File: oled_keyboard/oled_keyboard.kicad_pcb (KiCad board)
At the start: 2 copper layers, 125 x 125 mm, 123 parts, among them J1 Conn_01x20_Socket, J10 Conn_01x20_Socket, J11 Conn_01x20_Socket, J12 Conn_01x20_Socket, J2 Conn_01x20_Socket, J3 Conn_01x20_Socket, J4 Conn_01x20_Socket, J5 Conn_01x20_Socket, J6 Conn_01x20_Socket, J7 Conn_01x20_Socket, J8 Conn_01x20_Socket, J9 Conn_01x20_Socket, SW1 SW_Push, SW10 SW_Push, SW11 SW_Push, SW12 SW_Push, SW2 SW_Push, SW3 SW_Push, SW4 SW_Push, SW5 SW_Push, SW6 SW_Push, SW7 SW_Push, SW8 SW_Push, SW9 SW_Push, U1 TPS61088RHLR

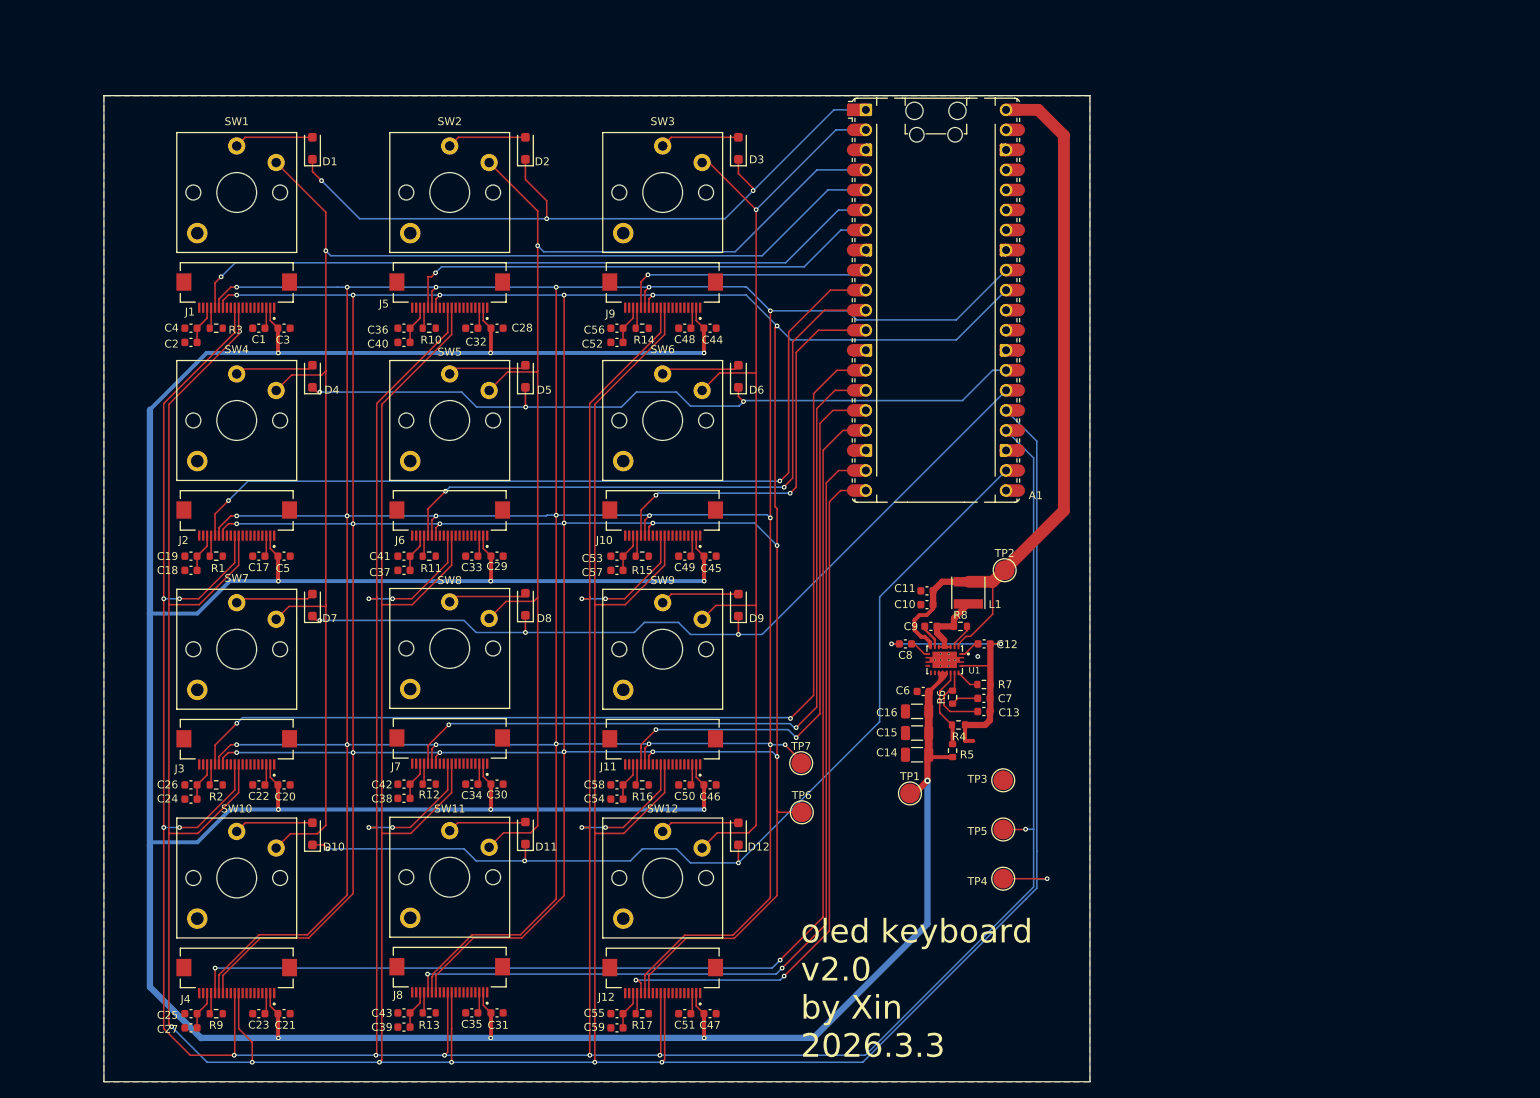
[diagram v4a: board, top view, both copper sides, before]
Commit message: chged to 9 oled. fixed pin inversion issue
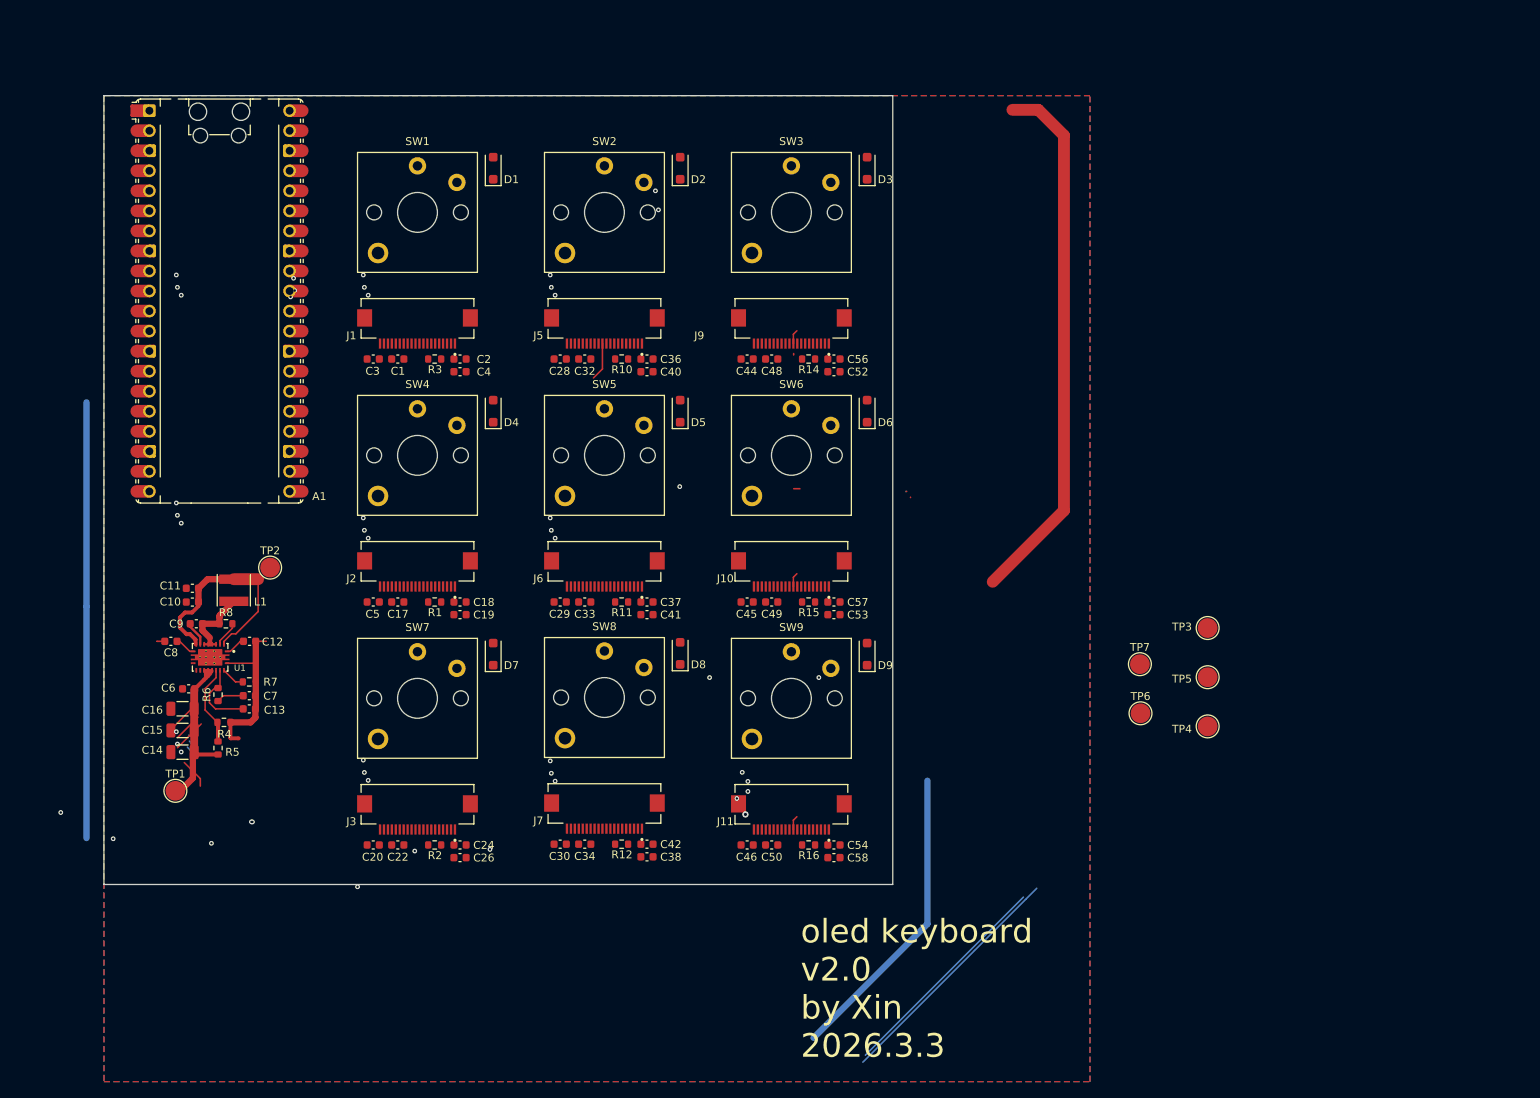
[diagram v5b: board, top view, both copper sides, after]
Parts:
- removed C21, C23, C31, C35, C47, C51: 4.7uF, Capacitor_SMD:C_0603_1608Metric
- removed C25, C39, C55: 0.1uF, Capacitor_SMD:C_0603_1608Metric
- removed C27, C43, C59: 1uF, Capacitor_SMD:C_0603_1608Metric
- removed D10, D11, D12: D, Diode_SMD:D_SOD-123F
- removed J12, J4, J8: Conn_01x20_Socket, 20p_connector:HRS_TF31-20S-0.5SH_800_
- removed R13, R17, R9: 1M, Resistor_SMD:R_0603_1608Metric
- removed SW10, SW11, SW12: SW_Push, Switch_Keyboard_Kailh:SW_Kailh_Choc_V1V2
- moved C10 93.1 mm to (93.1, 94.7)
- moved C11 93.1 mm to (93.1, 93.0)
- moved C12 93.1 mm to (100.3, 99.7)
- moved C13 93.1 mm to (100.3, 108.2)
- moved C14 93.1 mm to (91.8, 113.7)
- moved C15 93.1 mm to (91.8, 111.0)
- moved C16 93.1 mm to (91.8, 108.2)
- moved C7 93.1 mm to (100.3, 106.6)
- moved C9 93.1 mm to (93.6, 97.5)
- moved L1 93.1 mm to (98.3, 93.2)
- moved NT1 93.1 mm to (98.4, 112.0)
- moved R4 93.1 mm to (97.1, 110.0)
- moved R5 93.1 mm to (96.3, 113.2)
- moved R6 93.1 mm to (96.3, 106.4)
- moved R7 93.1 mm to (100.3, 104.8)
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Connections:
- C1 pad 1: Net-(J1-Pin_3) -> Net-(J1-Pin_18)
- C17 pad 1: Net-(J2-Pin_3) -> Net-(J2-Pin_18)
- C18 pad 1: Net-(J2-Pin_18) -> Net-(J2-Pin_3)
- C19 pad 1: Net-(J2-Pin_18) -> Net-(J2-Pin_3)
- C2 pad 1: Net-(J1-Pin_18) -> Net-(J1-Pin_3)
- C22 pad 1: Net-(J3-Pin_3) -> Net-(J3-Pin_18)
- C24 pad 1: Net-(J3-Pin_18) -> Net-(J3-Pin_3)
- C26 pad 1: Net-(J3-Pin_18) -> Net-(J3-Pin_3)
- C32 pad 1: Net-(J5-Pin_3) -> Net-(J5-Pin_18)
- C33 pad 1: Net-(J6-Pin_3) -> Net-(J6-Pin_18)
- C34 pad 1: Net-(J7-Pin_3) -> Net-(J7-Pin_18)
- C36 pad 1: Net-(J5-Pin_18) -> Net-(J5-Pin_3)
- C37 pad 1: Net-(J6-Pin_18) -> Net-(J6-Pin_3)
- C38 pad 1: Net-(J7-Pin_18) -> Net-(J7-Pin_3)
- C4 pad 1: Net-(J1-Pin_18) -> Net-(J1-Pin_3)
- C40 pad 1: Net-(J5-Pin_18) -> Net-(J5-Pin_3)
- C41 pad 1: Net-(J6-Pin_18) -> Net-(J6-Pin_3)
- C42 pad 1: Net-(J7-Pin_18) -> Net-(J7-Pin_3)
- C48 pad 1: Net-(J9-Pin_3) -> Net-(J9-Pin_18)
- C49 pad 1: Net-(J10-Pin_3) -> Net-(J10-Pin_18)
- C50 pad 1: Net-(J11-Pin_3) -> Net-(J11-Pin_18)
- C52 pad 1: Net-(J9-Pin_18) -> Net-(J9-Pin_3)
- C53 pad 1: Net-(J10-Pin_18) -> Net-(J10-Pin_3)
- C54 pad 1: Net-(J11-Pin_18) -> Net-(J11-Pin_3)
- C56 pad 1: Net-(J9-Pin_18) -> Net-(J9-Pin_3)
- C57 pad 1: Net-(J10-Pin_18) -> Net-(J10-Pin_3)
- C58 pad 1: Net-(J11-Pin_18) -> Net-(J11-Pin_3)
- J1 pad 10: /MOSI -> /SCK
- J1 pad 11: /SCK -> /MOSI
- J1 pad 14: /DC -> unconnected-(J1-Pin_14-Pad14)
- J1 pad 15: /RES -> unconnected-(J1-Pin_15-Pad15)
- J1 pad 16: /CS1 -> unconnected-(J1-Pin_16-Pad16)
- J1 pad 17: Net-(J1-Pin_17) -> unconnected-(J1-Pin_17-Pad17)
- J1 pad 19: unconnected-(J1-Pin_19-Pad19) -> VCC
- J1 pad 2: VCC -> unconnected-(J1-Pin_2-Pad2)
- J1 pad 4: unconnected-(J1-Pin_4-Pad4) -> Net-(J1-Pin_4)
- J1 pad 5: unconnected-(J1-Pin_5-Pad5) -> /CS1
- J1 pad 6: unconnected-(J1-Pin_6-Pad6) -> /RES
- J1 pad 7: unconnected-(J1-Pin_7-Pad7) -> /DC
- J10 pad 10: /MOSI -> /SCK
- J10 pad 11: /SCK -> /MOSI
- J10 pad 14: /DC -> unconnected-(J10-Pin_14-Pad14)
- J10 pad 15: /RES -> unconnected-(J10-Pin_15-Pad15)
- J10 pad 16: /CS6 -> unconnected-(J10-Pin_16-Pad16)
- J10 pad 17: Net-(J10-Pin_17) -> unconnected-(J10-Pin_17-Pad17)
- J10 pad 19: unconnected-(J10-Pin_19-Pad19) -> VCC
- J10 pad 2: VCC -> unconnected-(J10-Pin_2-Pad2)
- J10 pad 4: unconnected-(J10-Pin_4-Pad4) -> Net-(J10-Pin_4)
- J10 pad 5: unconnected-(J10-Pin_5-Pad5) -> /CS6
- J10 pad 6: unconnected-(J10-Pin_6-Pad6) -> /RES
- J10 pad 7: unconnected-(J10-Pin_7-Pad7) -> /DC
- J11 pad 10: /MOSI -> /SCK
- J11 pad 11: /SCK -> /MOSI
- J11 pad 14: /DC -> unconnected-(J11-Pin_14-Pad14)
- J11 pad 15: /RES -> unconnected-(J11-Pin_15-Pad15)
- J11 pad 16: /CS9 -> unconnected-(J11-Pin_16-Pad16)
- J11 pad 17: Net-(J11-Pin_17) -> unconnected-(J11-Pin_17-Pad17)
- J11 pad 19: unconnected-(J11-Pin_19-Pad19) -> VCC
- J11 pad 2: VCC -> unconnected-(J11-Pin_2-Pad2)
- J11 pad 4: unconnected-(J11-Pin_4-Pad4) -> Net-(J11-Pin_4)
- J11 pad 5: unconnected-(J11-Pin_5-Pad5) -> /CS9
- J11 pad 6: unconnected-(J11-Pin_6-Pad6) -> /RES
- J11 pad 7: unconnected-(J11-Pin_7-Pad7) -> /DC
- J2 pad 10: /MOSI -> /SCK
- J2 pad 11: /SCK -> /MOSI
- J2 pad 14: /DC -> unconnected-(J2-Pin_14-Pad14)
- J2 pad 15: /RES -> unconnected-(J2-Pin_15-Pad15)
- J2 pad 16: /CS4 -> unconnected-(J2-Pin_16-Pad16)
- J2 pad 17: Net-(J2-Pin_17) -> unconnected-(J2-Pin_17-Pad17)
- J2 pad 19: unconnected-(J2-Pin_19-Pad19) -> VCC
- J2 pad 2: VCC -> unconnected-(J2-Pin_2-Pad2)
- J2 pad 4: unconnected-(J2-Pin_4-Pad4) -> Net-(J2-Pin_4)
- J2 pad 5: unconnected-(J2-Pin_5-Pad5) -> /CS4
- J2 pad 6: unconnected-(J2-Pin_6-Pad6) -> /RES
- J2 pad 7: unconnected-(J2-Pin_7-Pad7) -> /DC
- J3 pad 10: /MOSI -> /SCK
- J3 pad 11: /SCK -> /MOSI
- J3 pad 14: /DC -> unconnected-(J3-Pin_14-Pad14)
- J3 pad 15: /RES -> unconnected-(J3-Pin_15-Pad15)
- J3 pad 16: /CS7 -> unconnected-(J3-Pin_16-Pad16)
- J3 pad 17: Net-(J3-Pin_17) -> unconnected-(J3-Pin_17-Pad17)
- J3 pad 19: unconnected-(J3-Pin_19-Pad19) -> VCC
- J3 pad 2: VCC -> unconnected-(J3-Pin_2-Pad2)
- J3 pad 4: unconnected-(J3-Pin_4-Pad4) -> Net-(J3-Pin_4)
- J3 pad 5: unconnected-(J3-Pin_5-Pad5) -> /CS7
- J3 pad 6: unconnected-(J3-Pin_6-Pad6) -> /RES
- J3 pad 7: unconnected-(J3-Pin_7-Pad7) -> /DC
- J5 pad 10: /MOSI -> /SCK
- J5 pad 11: /SCK -> /MOSI
- J5 pad 14: /DC -> unconnected-(J5-Pin_14-Pad14)
- J5 pad 15: /RES -> unconnected-(J5-Pin_15-Pad15)
- J5 pad 16: /CS2 -> unconnected-(J5-Pin_16-Pad16)
- J5 pad 17: Net-(J5-Pin_17) -> unconnected-(J5-Pin_17-Pad17)
- J5 pad 19: unconnected-(J5-Pin_19-Pad19) -> VCC
- J5 pad 2: VCC -> unconnected-(J5-Pin_2-Pad2)
- J5 pad 4: unconnected-(J5-Pin_4-Pad4) -> Net-(J5-Pin_4)
- J5 pad 5: unconnected-(J5-Pin_5-Pad5) -> /CS2
- J5 pad 6: unconnected-(J5-Pin_6-Pad6) -> /RES
- J5 pad 7: unconnected-(J5-Pin_7-Pad7) -> /DC
- J6 pad 10: /MOSI -> /SCK
- J6 pad 11: /SCK -> /MOSI
- J6 pad 14: /DC -> unconnected-(J6-Pin_14-Pad14)
- J6 pad 15: /RES -> unconnected-(J6-Pin_15-Pad15)
- J6 pad 16: /CS5 -> unconnected-(J6-Pin_16-Pad16)
- J6 pad 17: Net-(J6-Pin_17) -> unconnected-(J6-Pin_17-Pad17)
- J6 pad 19: unconnected-(J6-Pin_19-Pad19) -> VCC
- J6 pad 2: VCC -> unconnected-(J6-Pin_2-Pad2)
- J6 pad 4: unconnected-(J6-Pin_4-Pad4) -> Net-(J6-Pin_4)
- J6 pad 5: unconnected-(J6-Pin_5-Pad5) -> /CS5
- J6 pad 6: unconnected-(J6-Pin_6-Pad6) -> /RES
- J6 pad 7: unconnected-(J6-Pin_7-Pad7) -> /DC
- J7 pad 10: /MOSI -> /SCK
- J7 pad 11: /SCK -> /MOSI
- J7 pad 14: /DC -> unconnected-(J7-Pin_14-Pad14)
- J7 pad 15: /RES -> unconnected-(J7-Pin_15-Pad15)
- J7 pad 16: /CS8 -> unconnected-(J7-Pin_16-Pad16)
- J7 pad 17: Net-(J7-Pin_17) -> unconnected-(J7-Pin_17-Pad17)
- J7 pad 19: unconnected-(J7-Pin_19-Pad19) -> VCC
- J7 pad 2: VCC -> unconnected-(J7-Pin_2-Pad2)
- J7 pad 4: unconnected-(J7-Pin_4-Pad4) -> Net-(J7-Pin_4)
- J7 pad 5: unconnected-(J7-Pin_5-Pad5) -> /CS8
- J7 pad 6: unconnected-(J7-Pin_6-Pad6) -> /RES
- J7 pad 7: unconnected-(J7-Pin_7-Pad7) -> /DC
- J9 pad 10: /MOSI -> /SCK
- J9 pad 11: /SCK -> /MOSI
- J9 pad 14: /DC -> unconnected-(J9-Pin_14-Pad14)
- J9 pad 15: /RES -> unconnected-(J9-Pin_15-Pad15)
- J9 pad 16: /CS3 -> unconnected-(J9-Pin_16-Pad16)
- J9 pad 17: Net-(J9-Pin_17) -> unconnected-(J9-Pin_17-Pad17)
- J9 pad 19: unconnected-(J9-Pin_19-Pad19) -> VCC
- J9 pad 2: VCC -> unconnected-(J9-Pin_2-Pad2)
- J9 pad 4: unconnected-(J9-Pin_4-Pad4) -> Net-(J9-Pin_4)
- J9 pad 5: unconnected-(J9-Pin_5-Pad5) -> /CS3
- J9 pad 6: unconnected-(J9-Pin_6-Pad6) -> /RES
- J9 pad 7: unconnected-(J9-Pin_7-Pad7) -> /DC
- R1 pad 1: Net-(J2-Pin_17) -> Net-(J2-Pin_4)
- R10 pad 1: Net-(J5-Pin_17) -> Net-(J5-Pin_4)
- R11 pad 1: Net-(J6-Pin_17) -> Net-(J6-Pin_4)
- R12 pad 1: Net-(J7-Pin_17) -> Net-(J7-Pin_4)
- R14 pad 1: Net-(J9-Pin_17) -> Net-(J9-Pin_4)
- R15 pad 1: Net-(J10-Pin_17) -> Net-(J10-Pin_4)
- R16 pad 1: Net-(J11-Pin_17) -> Net-(J11-Pin_4)
- R2 pad 1: Net-(J3-Pin_17) -> Net-(J3-Pin_4)
- R3 pad 1: Net-(J1-Pin_17) -> Net-(J1-Pin_4)
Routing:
- net /RES: track 568.3 -> 3.82 mm, vias 19 -> 4
- net /MOSI: track 598.5 -> 36.0 mm, vias 7 -> 4
- net /DC: track 556.7 -> 0.00 mm, vias 18 -> 10
- net /SCK: track 594.2 -> 89.4 mm, vias 18 -> 9
- net VCC: track 513.8 -> 62.3 mm, vias 13 -> 2
- net /COL1: track 180.8 -> 0.00 mm, vias 1 -> 0
- net /COL2: track 154.4 -> 0.00 mm, vias 1 -> 0
- net /CS10: track 147.8 -> 0.00 mm, vias 2 -> 0
- net /COL3: track 128.8 -> 0.00 mm
- net /CS7: track 126.5 -> 0.00 mm, vias 2 -> 1
- net /ROW4: track 124.5 -> 0.00 mm, vias 3 -> 2
- net /CS11: track 116.4 -> 0.18 mm, vias 2 -> 1
- net /ROW3: track 107.3 -> 0.00 mm, vias 3 -> 0
- net /CS4: track 106.6 -> 0.00 mm, vias 2 -> 1
- net /ROW2: track 96.9 -> 0.00 mm, vias 3 -> 0
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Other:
- board size 125 x 125 mm -> 100 x 100 mm

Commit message: optimized key layout
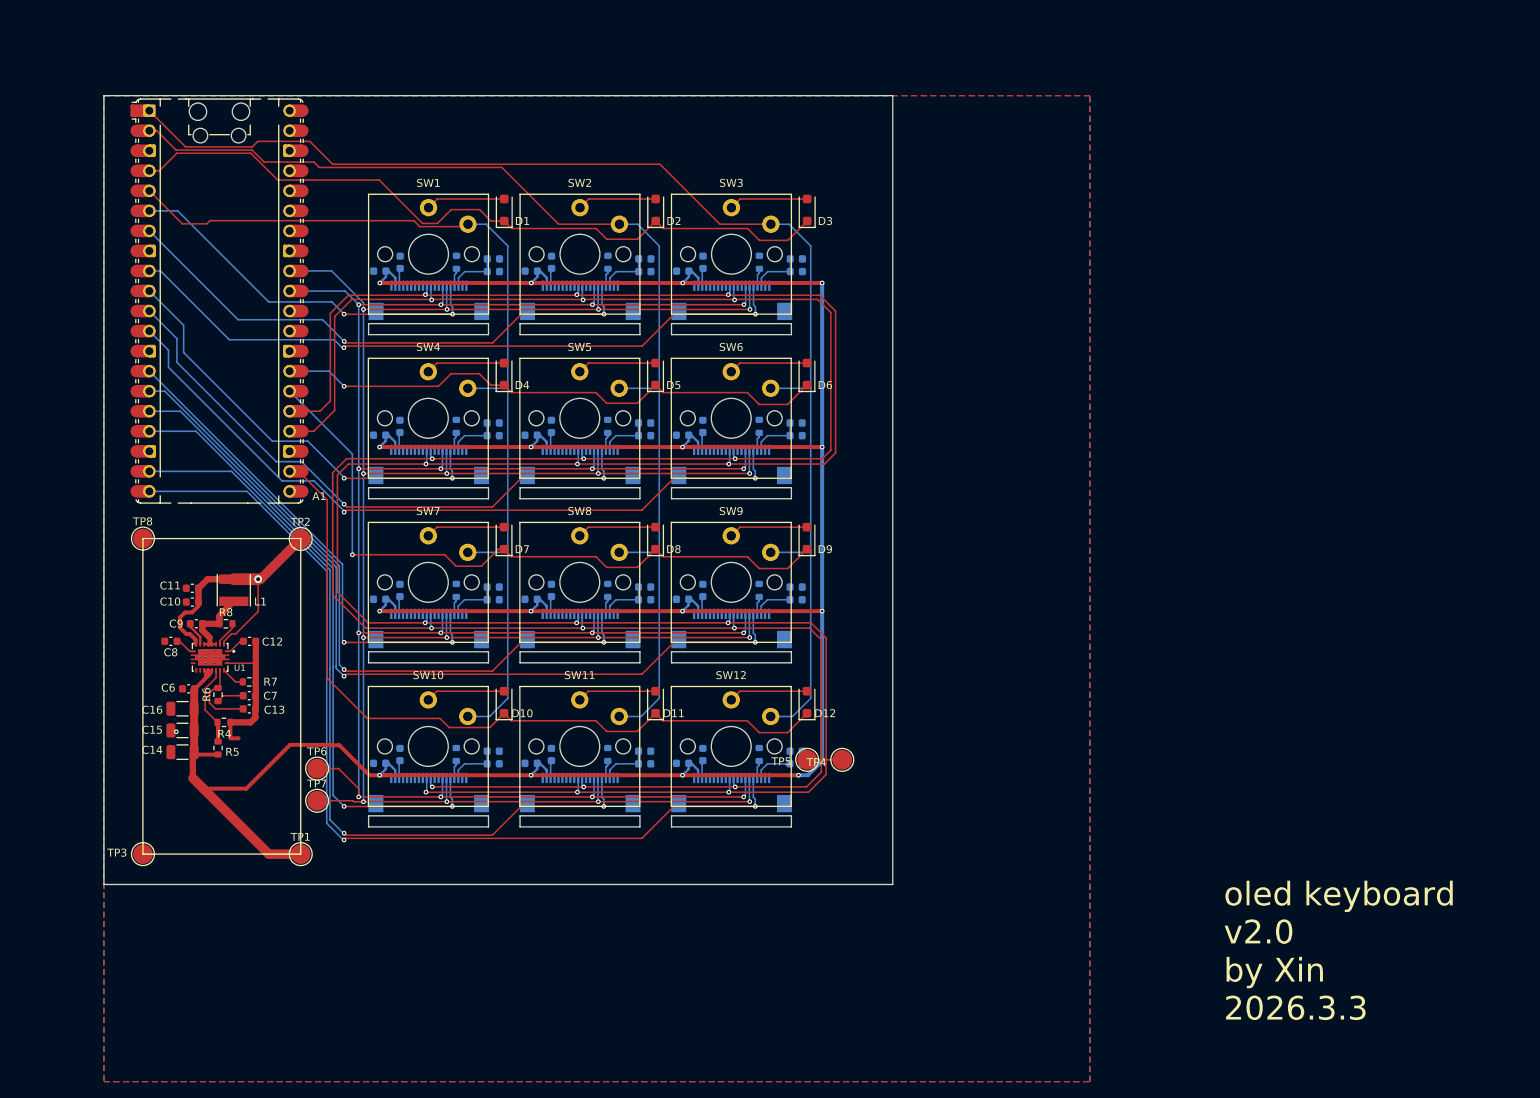
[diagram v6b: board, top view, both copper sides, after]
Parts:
- added C21: 1uF, Capacitor_SMD:C_0603_1608Metric, B.Cu at (131.2, 113.6)
- added C23: 0.1uF, Capacitor_SMD:C_0603_1608Metric, B.Cu at (131.2, 115.2)
- added C25: 4.7uF, Capacitor_SMD:C_0603_1608Metric, B.Cu at (119.4, 114.0)
- added C27: 4.7uF, Capacitor_SMD:C_0603_1608Metric, B.Cu at (116.8, 115.1)
- added C31: 1uF, Capacitor_SMD:C_0603_1608Metric, B.Cu at (150.4, 113.6)
- added C35: 0.1uF, Capacitor_SMD:C_0603_1608Metric, B.Cu at (150.4, 115.2)
- added C39: 4.7uF, Capacitor_SMD:C_0603_1608Metric, B.Cu at (138.6, 114.0)
- added C43: 4.7uF, Capacitor_SMD:C_0603_1608Metric, B.Cu at (136.0, 115.1)
- added C47: 1uF, Capacitor_SMD:C_0603_1608Metric, B.Cu at (169.6, 113.6)
- added C51: 0.1uF, Capacitor_SMD:C_0603_1608Metric, B.Cu at (169.6, 115.2)
- added C55: 4.7uF, Capacitor_SMD:C_0603_1608Metric, B.Cu at (157.8, 114.0)
- added C59: 4.7uF, Capacitor_SMD:C_0603_1608Metric, B.Cu at (155.2, 115.1)
- added D10: D, Diode_SMD:D_SOD-123F, F.Cu at (132.6, 107.4)
- added D11: D, Diode_SMD:D_SOD-123F, F.Cu at (151.8, 107.4)
- added D12: D, Diode_SMD:D_SOD-123F, F.Cu at (171.0, 107.4)
- added J12: Conn_01x20_Socket, 20pin_connector:HRS_TF31-20S-0.5SH_800_, B.Cu at (161.4, 120.2)
- added J4: Conn_01x20_Socket, 20pin_connector:HRS_TF31-20S-0.5SH_800_, B.Cu at (123.0, 120.2)
- added J8: Conn_01x20_Socket, 20pin_connector:HRS_TF31-20S-0.5SH_800_, B.Cu at (142.2, 120.2)
- added R13: 1M, Resistor_SMD:R_0603_1608Metric, B.Cu at (145.7, 114.0)
- added R17: 1M, Resistor_SMD:R_0603_1608Metric, B.Cu at (164.9, 114.0)
- added R9: 1M, Resistor_SMD:R_0603_1608Metric, B.Cu at (126.5, 114.0)
- added SW10: SW_Push, keyboard_custom:SW_Kailh_Choc_V1V2, F.Cu at (123.0, 113.0)
- added SW11: SW_Push, keyboard_custom:SW_Kailh_Choc_V1V2, F.Cu at (142.2, 113.0)
- added SW12: SW_Push, keyboard_custom:SW_Kailh_Choc_V1V2, F.Cu at (161.4, 113.0)
- added TP8: TestPoint, TestPoint:TestPoint_Pad_D2.5mm, F.Cu at (86.8, 86.7)
- C1, C17, C18, C19, C2, C20, C22, C24, C26, C28, C29, C3, C30, C32, C33, C34, C36, C37, C38, C4, C40, C41, C42, C44, C45, C46, C48, C49, C5, C50, C52, C53, C54, C56, C57, C58, J10, J11, J2, J3, J5, J6, J7, J9, R1, R10, R11, R12, R14, R15, R16, R2, R3: moved to B.Cu
- J1: footprint 20p_connector:HRS_TF31-20S-0.5SH_800_ -> 20pin_connector:HRS_TF31-20S-0.5SH_800_; moved to B.Cu
- SW1, SW2, SW3, SW4, SW5, SW6, SW7, SW8, SW9: footprint Switch_Keyboard_Kailh:SW_Kailh_Choc_V1V2 -> keyboard_custom:SW_Kailh_Choc_V1V2
- moved TP3 138.0 mm to (86.8, 126.7)
- moved TP7 105.7 mm to (108.9, 119.9)
- moved TP6 104.6 mm to (108.9, 115.8)
- moved TP5 51.8 mm to (171.0, 114.7)
- moved TP4 46.5 mm to (175.4, 114.7)
- moved C58 34.6 mm to (169.6, 92.8)
- moved C26 34.6 mm to (131.2, 92.8)
- moved C50 33.4 mm to (157.8, 93.2), turned to 90 degrees
- moved R16 32.9 mm to (164.9, 93.2), turned to 90 degrees
- moved C38 32.6 mm to (150.4, 94.4)
- moved C42 32.6 mm to (150.4, 92.8)
- moved C34 32.4 mm to (138.6, 93.2), turned to 90 degrees
- moved R2 32.4 mm to (126.5, 93.2), turned to 90 degrees
- moved C22 32.3 mm to (119.4, 93.2), turned to 90 degrees
- moved R12 32.2 mm to (145.7, 93.2), turned to 90 degrees
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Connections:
- A1 pad 1: /ROW1 -> /COL3
- A1 pad 2: /COL3 -> /COL2
- A1 pad 4: /COL2 -> /ROW1
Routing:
- net VCC: track 62.3 -> 406.1 mm, vias 2 -> 16
- net /RES: track 3.82 -> 312.4 mm, vias 4 -> 16
- net /DC: track 0.00 -> 304.5 mm, vias 10 -> 16
- net /MOSI: track 36.0 -> 332.7 mm, vias 4 -> 12
- net /SCK: track 89.4 -> 331.0 mm, vias 9 -> 12
- net /COL3: track 0.00 -> 165.1 mm, vias 1 -> 0
- net /COL2: track 0.00 -> 144.2 mm
- net /COL1: track 0.00 -> 122.5 mm
- net /CS12: track 0.80 -> 119.3 mm, vias 0 -> 2
- net /CS11: track 0.18 -> 100.5 mm, vias 1 -> 2
- net /CS9: track 5.85 -> 103.7 mm, vias 3 -> 2
- net /ROW4: track 0.00 -> 97.0 mm, vias 2 -> 0
- net /ROW1: track 0.00 -> 93.3 mm, vias 1 -> 0
- net /CS6: track 4.33 -> 93.2 mm, vias 1 -> 2
- net /ROW3: track 0.00 -> 87.1 mm, vias 0 -> 1
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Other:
- outline, holes or cut-outs redrawn
- copper layers 2 -> 4

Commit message: v3.0
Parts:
- added R18: 33R, Resistor_SMD:R_0603_1608Metric, F.Cu at (111.9, 68.0)
- added R19: 33R, Resistor_SMD:R_0603_1608Metric, F.Cu at (109.7, 68.0)
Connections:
- J1 pad 10: /SCK -> /SCLK
- J1 pad 11: /MOSI -> /SDIN
- J10 pad 10: /SCK -> /SCLK
- J10 pad 11: /MOSI -> /SDIN
- J11 pad 10: /SCK -> /SCLK
- J11 pad 11: /MOSI -> /SDIN
- J12 pad 10: /SCK -> /SCLK
- J12 pad 11: /MOSI -> /SDIN
- J2 pad 10: /SCK -> /SCLK
- J2 pad 11: /MOSI -> /SDIN
- J3 pad 10: /SCK -> /SCLK
- J3 pad 11: /MOSI -> /SDIN
- J4 pad 10: /SCK -> /SCLK
- J4 pad 11: /MOSI -> /SDIN
- J5 pad 10: /SCK -> /SCLK
- J5 pad 11: /MOSI -> /SDIN
- J6 pad 10: /SCK -> /SCLK
- J6 pad 11: /MOSI -> /SDIN
- J7 pad 10: /SCK -> /SCLK
- J7 pad 11: /MOSI -> /SDIN
- J8 pad 10: /SCK -> /SCLK
- J8 pad 11: /MOSI -> /SDIN
- J9 pad 10: /SCK -> /SCLK
- J9 pad 11: /MOSI -> /SDIN
- TP4 pad 1: /MOSI -> /SDIN
- TP5 pad 1: /SCK -> /SCLK
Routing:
- net /MOSI: track 332.7 -> 4.88 mm, vias 12 -> 0
- net /SDIN: track 0.00 -> 326.8 mm, vias 0 -> 12
- net /SCLK: track 0.00 -> 323.0 mm, vias 0 -> 12
- net /SCK: track 331.0 -> 8.62 mm, vias 12 -> 0
- net AGND: track 21.6 -> 38.7 mm, vias 0 -> 2
- net VCC: track 406.1 -> 408.4 mm
- net VBUS: track 104.1 -> 103.0 mm
- net /RES: track 312.4 -> 313.1 mm
- net /DC: track 304.5 -> 303.9 mm
- added copper zone on In1.Cu, net GND
- added copper zone on In2.Cu, net GND
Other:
- board text added: "oled keyboard v3.0 by Xin 2026.5.26"
- board text removed: "oled keyboard v2.0 by Xin 2026.3.3"
